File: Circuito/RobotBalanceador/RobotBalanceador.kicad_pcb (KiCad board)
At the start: 2 copper layers, 70 x 45 mm, 62 parts, among them J1 ICSP, J2 USB_B_Micro, J3 Barrel_Jack_Switch, J4 ENCODER, J5 ENCODER, J6 MOT 1, J7 MOT 2, U1 STM32F103C8Tx, U2 LMR62014XMF, U3 AMS1117-3.3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

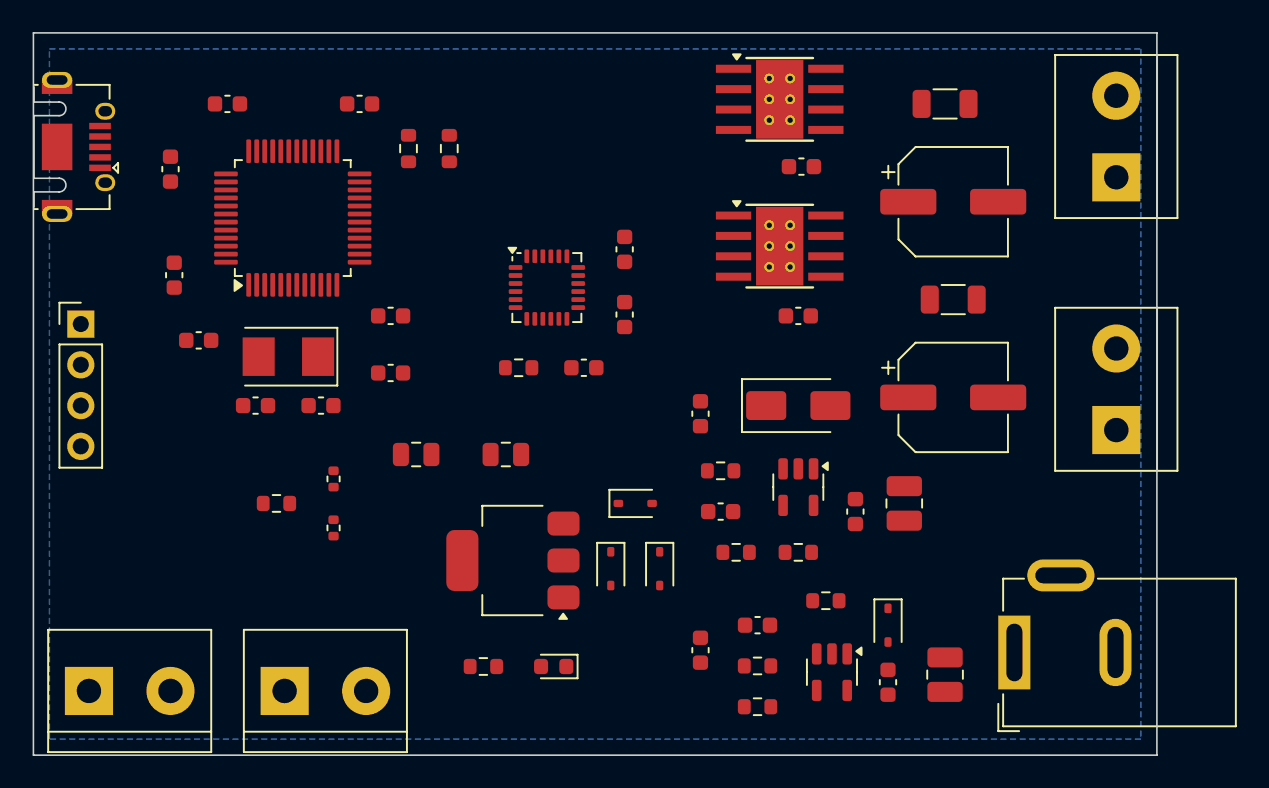
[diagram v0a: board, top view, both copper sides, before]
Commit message: Ruteado inicial de tracks
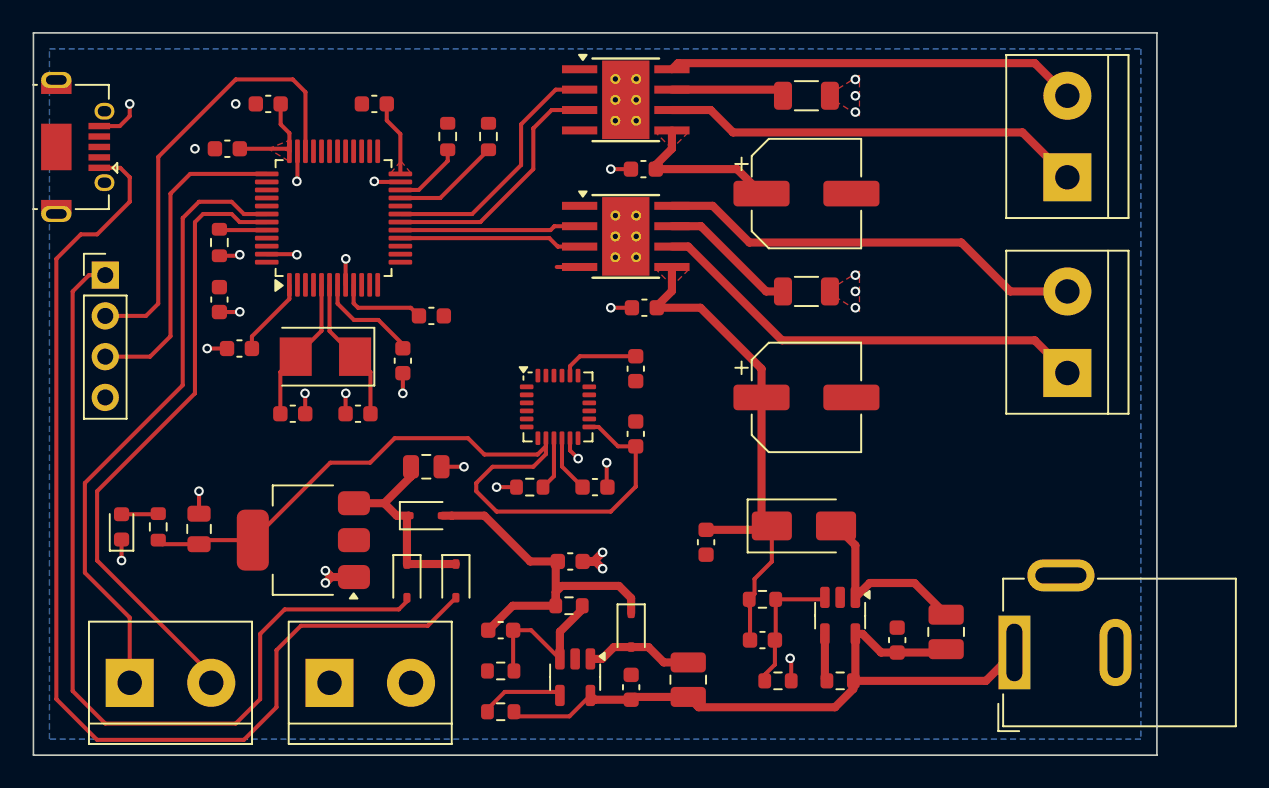
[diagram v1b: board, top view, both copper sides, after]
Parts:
- removed R13, R14: 0R, Resistor_SMD:R_0402_1005Metric
- moved D6 28.3 mm to (126.5, 116.8), turned to 90 degrees
- moved R15 22.0 mm to (128.8, 116.8), turned to -90 degrees
- moved R1 16.6 mm to (132.6, 99.1), turned to 90 degrees
- moved C15 16.0 mm to (158.2, 126.8)
- moved C16 16.0 mm to (150.1, 123.2)
- moved D3 16.0 mm to (158.2, 123.2)
- moved L2 16.0 mm to (161.8, 126.3)
- moved R5 16.0 mm to (150.1, 128.3)
- moved R6 16.0 mm to (150.1, 125.8)
- moved R7 16.0 mm to (154.4, 121.7)
- moved U4 16.0 mm to (154.8, 126.1)
- moved C11 14.3 mm to (131.3, 116.9), turned to 90 degrees
- moved U3 13.1 mm to (137.8, 117.6)
- moved D1 13.1 mm to (145.4, 116.1)
- moved D2 12.7 mm to (144.3, 120.1)
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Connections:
- net Net-(D6-A) renamed /LED_ANODE
- C16 pad 1: /LMR1_FB -> /LMR2_FB
- J5 pad 1: +5V -> +5V_CONV
- R1 pad 1: /JP_BOOT0 -> GND
- R6 pad 2: /LMR1_FB -> /LMR2_FB
- R7 pad 1: /LMR1_FB -> /LMR2_FB
- U4 pad 3: /LMR1_FB -> /LMR2_FB
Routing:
- net +3V3: track 0.00 -> 74.9 mm
- net VBUS: track 0.00 -> 68.8 mm
- net +5V: track 0.00 -> 54.8 mm
- net +BATT: track 0.00 -> 43.2 mm
- net +12V: track 0.00 -> 43.0 mm
- net /ENC_B: track 0.00 -> 39.1 mm
- net /ENC_A: track 0.00 -> 38.6 mm
- net GND: track 0.00 -> 35.4 mm, vias 0 -> 32
- net /SWDIO: track 0.00 -> 27.9 mm
- net /MOT2_A: track 0.00 -> 27.9 mm
- net /MOT2_B: track 0.00 -> 26.8 mm
- net /MOT1_A: track 0.00 -> 26.4 mm
- net /MOT1_B: track 0.00 -> 25.6 mm
- net +5V_CONV: track 0.00 -> 23.0 mm
- net /SWCLK: track 0.00 -> 20.0 mm
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- added copper zone on F.Cu, net +12V
- added copper zone on F.Cu, net +3V3
- added copper zone on F.Cu, net GND

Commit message: Ruteado completo, gerbers generados
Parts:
- added R11: 1.5k, Resistor_SMD:R_0603_1608Metric, F.Cu at (139.2, 90.4)
- added kibuzzard-66D679E5: G***, kibuzzard-66D679E5, F.Cu at (129.0, 111.8)
- added kibuzzard-66D679E8: G***, kibuzzard-66D679E8, F.Cu at (129.0, 106.7)
- added kibuzzard-66D679EB: G***, kibuzzard-66D679EB, F.Cu at (129.0, 109.2)
- added kibuzzard-66D679FF: G***, kibuzzard-66D679FF, F.Cu at (129.0, 120.4)
- added kibuzzard-66D67A08: G***, kibuzzard-66D67A08, F.Cu at (134.1, 120.4)
- added kibuzzard-66D67A11: G***, kibuzzard-66D67A11, F.Cu at (139.2, 120.4)
- added kibuzzard-66D67A2F: G***, kibuzzard-66D67A2F, F.Cu at (176.8, 105.7)
- added kibuzzard-66D67A48: G***, kibuzzard-66D67A48, F.Cu at (154.4, 105.4)
- added kibuzzard-66D67A51: G***, kibuzzard-66D67A51, F.Cu at (151.6, 102.6)
- added kibuzzard-66D67A84: G***, kibuzzard-66D67A84, F.Cu at (176.8, 93.5)
- added kibuzzard-66D67EE6: G***, kibuzzard-66D67EE6, F.Cu at (151.9, 120.4)
- added kibuzzard-66D67F1F: G***, kibuzzard-66D67F1F, F.Cu at (129.0, 104.1)
- D4: value SS22 -> 1N5819WS; footprint Diode_SMD:D_SMA -> Diode_SMD:D_SOD-323
- J2: footprint Connector_USB:USB_Micro-AB_Molex_47590-0001 -> Connector_USB:USB_Micro-B_Molex-105017-0001
- moved L1 11.3 mm to (170.5, 114.8), turned to 180 degrees
- moved J3 7.73 mm to (176.4, 119.4)
- moved C13 4.99 mm to (171.8, 119.9)
- moved J4 4.06 mm to (131.1, 126.5)
- moved R4 3.92 mm to (164.8, 123.4)
- moved C14 3.92 mm to (163.8, 120.9)
- moved R3 3.92 mm to (168.7, 123.4)
- moved U2 3.92 mm to (168.7, 119.4)
- moved R2 3.92 mm to (163.8, 118.4)
- moved C12 3.82 mm to (160.5, 114.8)
- moved C16 3.75 mm to (153.9, 123.2)
- moved R5 3.75 mm to (153.9, 128.3)
- moved R6 3.75 mm to (153.9, 125.8)
- moved D4 3.73 mm to (166.4, 114.0)
- moved J2 3.64 mm to (123.8, 96.5)
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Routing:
- net +3V3: track 74.9 -> 147.9 mm, vias 0 -> 3
- net +12V: track 43.0 -> 101.7 mm
- net GND: track 35.4 -> 73.7 mm, vias 32 -> 41
- net /USB_D-: track 0.00 -> 23.4 mm
- net /USB_D+: track 0.00 -> 22.4 mm
- net /I2C_SDA: track 4.40 -> 26.5 mm, vias 0 -> 2
- net /I2C_SCL: track 6.73 -> 26.5 mm, vias 0 -> 2
- net +5V_CONV: track 23.0 -> 37.3 mm
- net +BATT: track 43.2 -> 35.1 mm
- net /LMR1_SW: track 11.8 -> 5.80 mm
- net +5V: track 54.8 -> 49.4 mm
- net /ENC_B: track 39.1 -> 43.9 mm
- net VBUS: track 68.8 -> 64.3 mm
- net /ENC_A: track 38.6 -> 42.4 mm
- net /SWCLK: track 20.0 -> 23.5 mm
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- removed copper zone on F.Cu, net GND
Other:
- board text added: "JLCJLCJLCJLC"

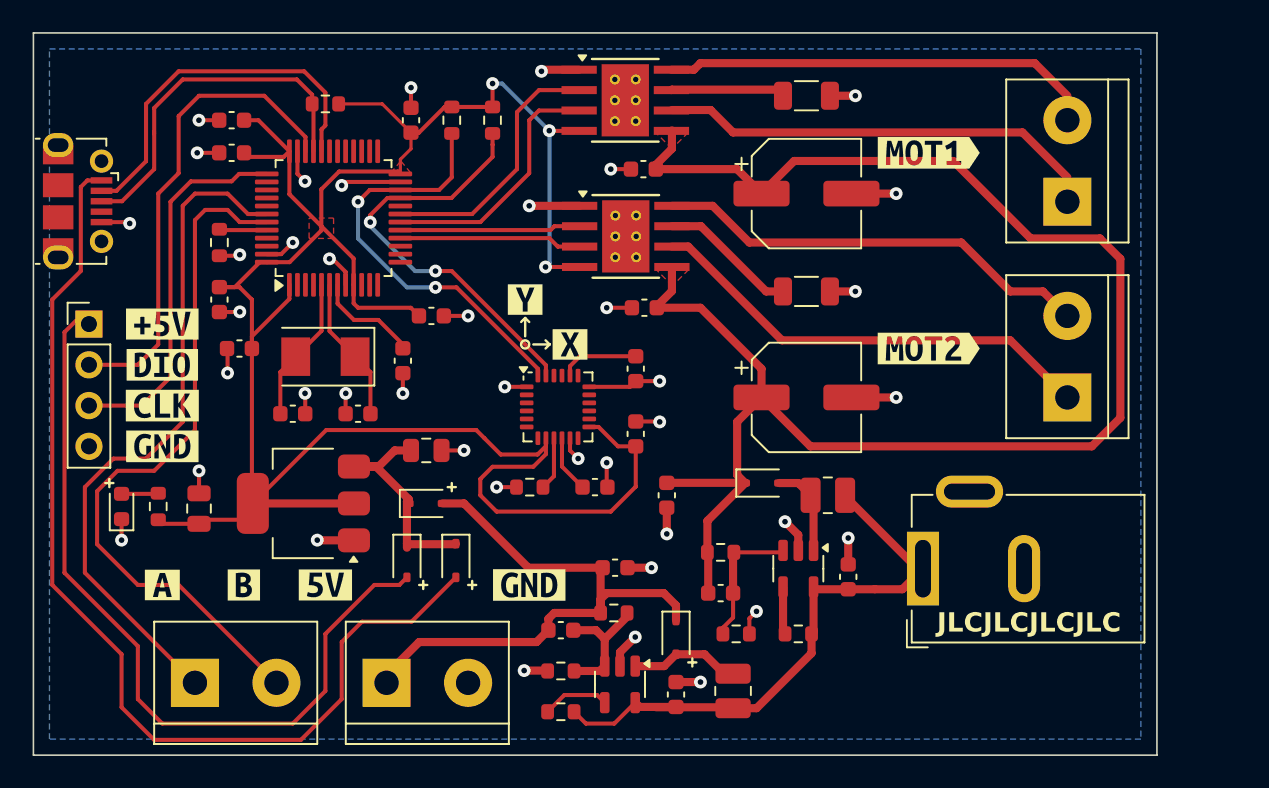
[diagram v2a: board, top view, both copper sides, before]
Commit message: Modificaciones a USB y ruteado
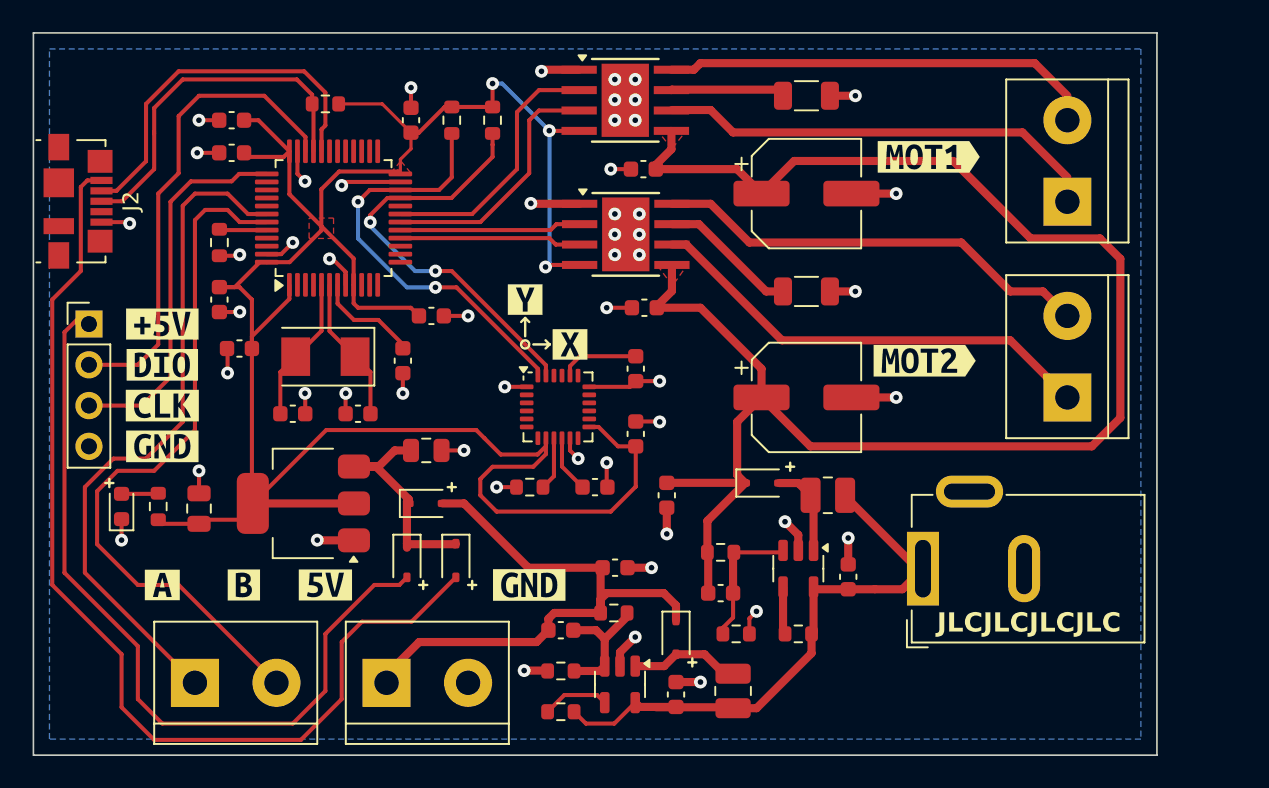
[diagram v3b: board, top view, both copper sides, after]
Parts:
- J2: footprint Connector_USB:USB_Micro-B_Molex-105017-0001 -> Connector_USB:USB_Micro-B_Molex_47346-0001
- moved kibuzzard-66D67A2F 0.80 mm to (176.5, 106.4)
- moved kibuzzard-66D67A84 0.25 mm to (176.8, 93.7)
- moved U7 0.13 mm to (157.9, 98.6)
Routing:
- net GND: track 73.7 -> 73.6 mm, vias 41 -> 53
